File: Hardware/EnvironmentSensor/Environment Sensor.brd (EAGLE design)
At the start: 34 x 57 mm, 18 parts, among them IC1 ATMEGA328P-AU, Q1 8MHz

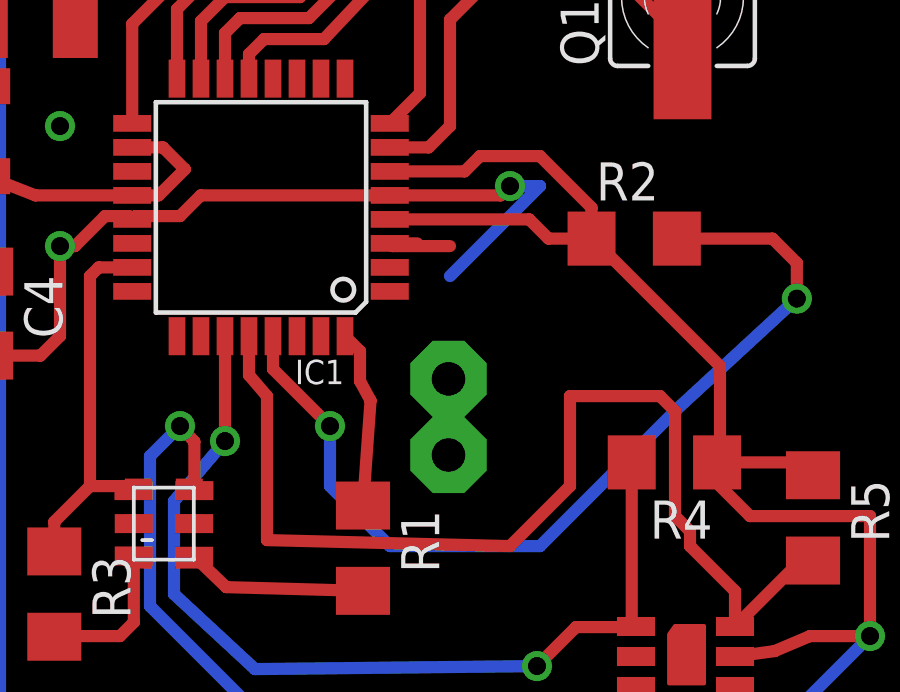
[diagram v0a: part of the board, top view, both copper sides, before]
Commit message: updated etch and create TOP etch for print tests
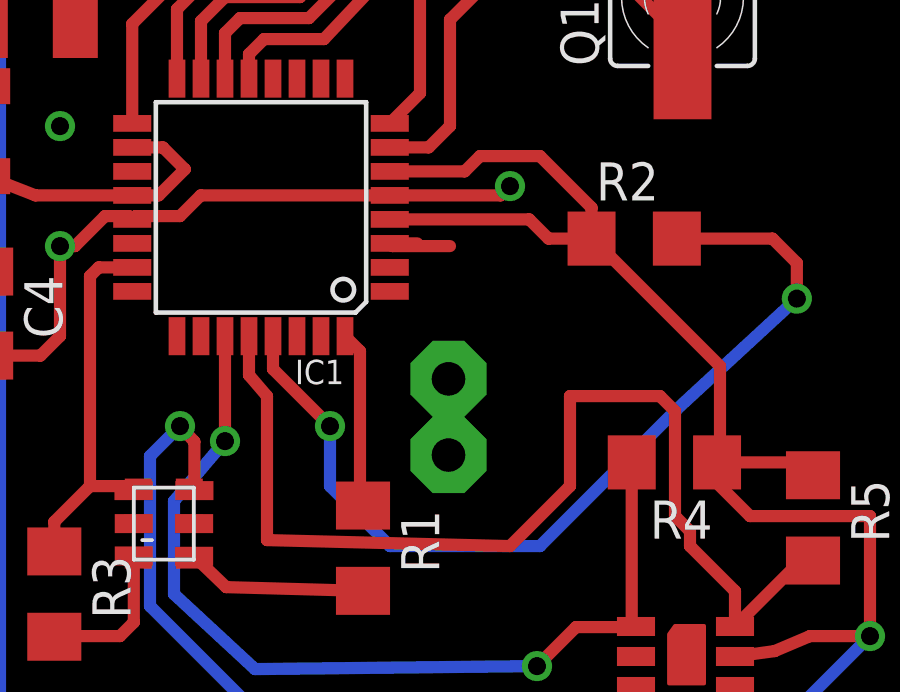
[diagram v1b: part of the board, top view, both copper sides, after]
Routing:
- net GND: track 34.9 -> 29.7 mm
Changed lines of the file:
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@@
 <layer number="14" name="Route14" color="1" fill="6" visible="no" active="no"/>
 <layer number="15" name="Route15" color="4" fill="6" visible="no" active="no"/>
-<layer number="16" name="Bottom" color="1" fill="1" visible="yes" active="yes"/>
+<layer number="16" name="Bottom" color="1" fill="1" visible="no" active="yes"/>
 <layer number="17" name="Pads" color="2" fill="1" visible="yes" active="yes"/>
 <layer number="18" name="Vias" color="2" fill="1" visible="yes" active="yes"/>
 <layer number="19" name="Unrouted" color="6" fill="1" visible="yes" active="yes"/>
 <layer number="20" name="Dimension" color="15" fill="1" visible="yes" active="yes"/>
-<layer number="21" name="tPlace" color="7" fill="1" visible="yes" active="yes"/>
-<layer number="22" name="bPlace" color="7" fill="1" visible="yes" active="yes"/>
-<layer number="23" name="tOrigins" color="15" fill="1" visible="yes" active="yes"/>
-<layer number="24" name="bOrigins" color="15" fill="1" visible="yes" active="yes"/>
+<layer number="21" name="tPlace" color="7" fill="1" visible="no" active="yes"/>
+<layer number="22" name="bPlace" color="7" fill="1" visible="no" active="yes"/>
+<layer number="23" name="tOrigins" color="15" fill="1" visible="no" active="yes"/>
+<layer number="24" name="bOrigins" color="15" fill="1" visible="no" active="yes"/>
 <layer number="25" name="tNames" color="7" fill="1" visible="no" active="yes"/>
 <layer number="26" name="bNames" color="7" fill="1" visible="no" active="yes"/>
@@
 </polygon>
 <wire x1="16.9926" y1="33.09" x2="17.91" y2="33.09" width="0.4064" layer="1"/>
-<wire x1="19" y1="32" x2="22" y2="35" width="0.4064" layer="16"/>
-<wire x1="22" y1="35" x2="21" y2="35" width="0.4064" layer="16"/>
 <via x="21" y="35" extent="1-16" drill="0.6" shape="square"/>
 <wire x1="20.69" y1="34.69" x2="21" y2="35" width="0.4064" layer="1"/>
@@
 <contactref element="IC1" pad="32"/>
 <wire x1="15.5" y1="29.9974" x2="16" y2="29.4974" width="0.4064" layer="1"/>
-<wire x1="16" y1="29.4974" x2="16" y2="28.5" width="0.4064" layer="1"/>
-<wire x1="16" y1="28.5" x2="16.352" y2="27.852" width="0.4064" layer="1"/>
-<wire x1="16.352" y1="27.852" x2="16.1" y2="24.352" width="0.4064" layer="1"/>
+<wire x1="16.1" y1="24.352" x2="16" y2="24.352" width="0.4064" layer="1"/>
+<wire x1="16" y1="24.352" x2="16" y2="29.4974" width="0.4064" layer="1"/>
 </signal>
 <signal name="SDA">

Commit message: updated component Values
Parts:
- C3: value 0.1u -> 1u
- C4: value (none) -> 100n
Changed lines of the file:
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@@
 <layer number="19" name="Unrouted" color="6" fill="1" visible="yes" active="yes"/>
 <layer number="20" name="Dimension" color="15" fill="1" visible="yes" active="yes"/>
-<layer number="21" name="tPlace" color="7" fill="1" visible="no" active="yes"/>
+<layer number="21" name="tPlace" color="7" fill="1" visible="yes" active="yes"/>
 <layer number="22" name="bPlace" color="7" fill="1" visible="no" active="yes"/>
-<layer number="23" name="tOrigins" color="15" fill="1" visible="no" active="yes"/>
+<layer number="23" name="tOrigins" color="15" fill="1" visible="yes" active="yes"/>
 <layer number="24" name="bOrigins" color="15" fill="1" visible="no" active="yes"/>
-<layer number="25" name="tNames" color="7" fill="1" visible="no" active="yes"/>
+<layer number="25" name="tNames" color="7" fill="1" visible="yes" active="yes"/>
 <layer number="26" name="bNames" color="7" fill="1" visible="no" active="yes"/>
 <layer number="27" name="tValues" color="7" fill="1" visible="no" active="yes"/>
@@
 <layer number="46" name="Milling" color="3" fill="1" visible="no" active="yes"/>
 <layer number="47" name="Measures" color="7" fill="1" visible="no" active="yes"/>
-<layer number="48" name="Document" color="7" fill="1" visible="no" active="yes"/>
-<layer number="49" name="Reference" color="7" fill="1" visible="no" active="yes"/>
+<layer number="48" name="Document" color="7" fill="1" visible="yes" active="yes"/>
+<layer number="49" name="Reference" color="7" fill="1" visible="yes" active="yes"/>
 <layer number="50" name="dxf" color="7" fill="1" visible="no" active="no"/>
-<layer number="51" name="tDocu" color="7" fill="1" visible="no" active="yes"/>
-<layer number="52" name="bDocu" color="7" fill="1" visible="no" active="yes"/>
+<layer number="51" name="tDocu" color="7" fill="1" visible="yes" active="yes"/>
+<layer number="52" name="bDocu" color="7" fill="1" visible="yes" active="yes"/>
 <layer number="91" name="Nets" color="2" fill="1" visible="no" active="no"/>
 <layer number="92" name="Busses" color="1" fill="1" visible="no" active="no"/>
@@
 <element name="G1" library="battery" package="B2430UNI" value="B2430UNI" x="18.95" y="20.32" rot="MR180"/>
 <element name="R2" library="rcl" package="R1206" value="10k" x="25.14" y="33.25"/>
-<element name="C3" library="rcl" package="C1206K" value="0.1u" x="5.01" y="40.27"/>
+<element name="C3" library="rcl" package="C1206K" value="1u" x="5.01" y="40.27"/>
 <element name="L1" library="rcl" package="L3216C" value="10u" x="3.54" y="36.83" rot="R90"/>
-<element name="C4" library="rcl" package="C1206" value="" x="3.54" y="30.75" rot="R270"/>
+<element name="C4" library="rcl" package="C1206" value="100n" x="3.54" y="30.75" rot="R270"/>
 <element name="G2" library="battery" package="SL-160AA/PR" value="SL-160AA/PR" x="11.57" y="29.21" rot="MR90"/>
 <element name="G3" library="battery" package="SL-160AA/PR" value="SL-160AA/PR" x="26.83" y="29.21" rot="MR270"/>
